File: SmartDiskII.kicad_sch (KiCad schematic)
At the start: 42 parts, among them J1 Apple II Expansion Slot, J2 DRV, U1 74LS174, U10 27C256, U11 74LS245, U12 74LS323, U13 74LS00, U14 74LS174, U2 NE556, U3 74LS05, U4 74LS132, U5 74LS259/9334, U6 74LS20, U7 74LS21, U8 2758/16/32 P6, U9 74LS30

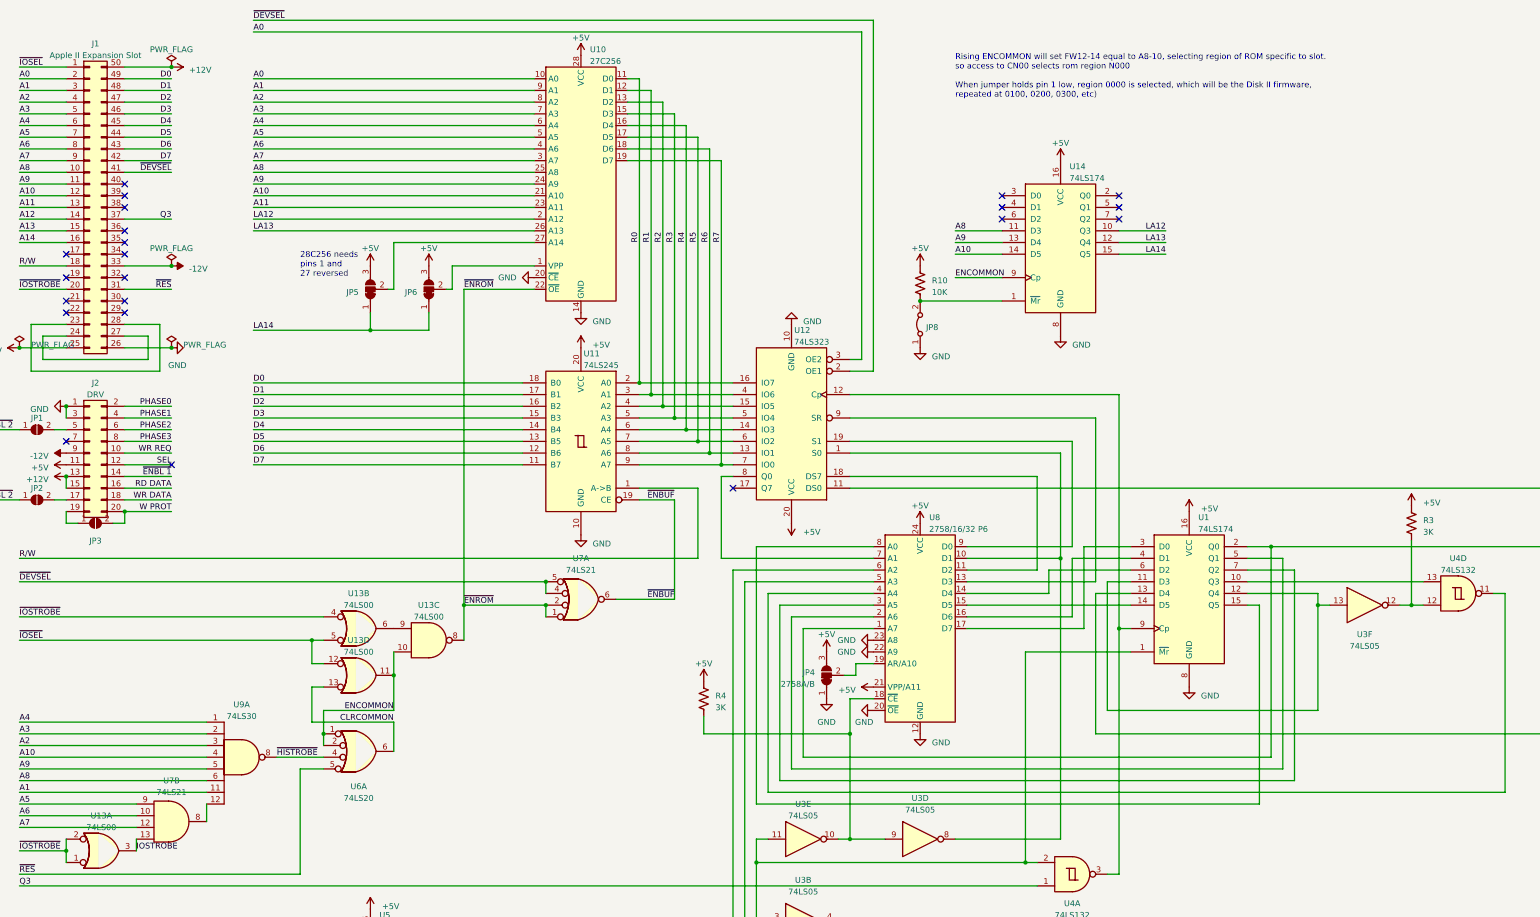
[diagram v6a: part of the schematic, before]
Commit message: fix jumper, tweaks
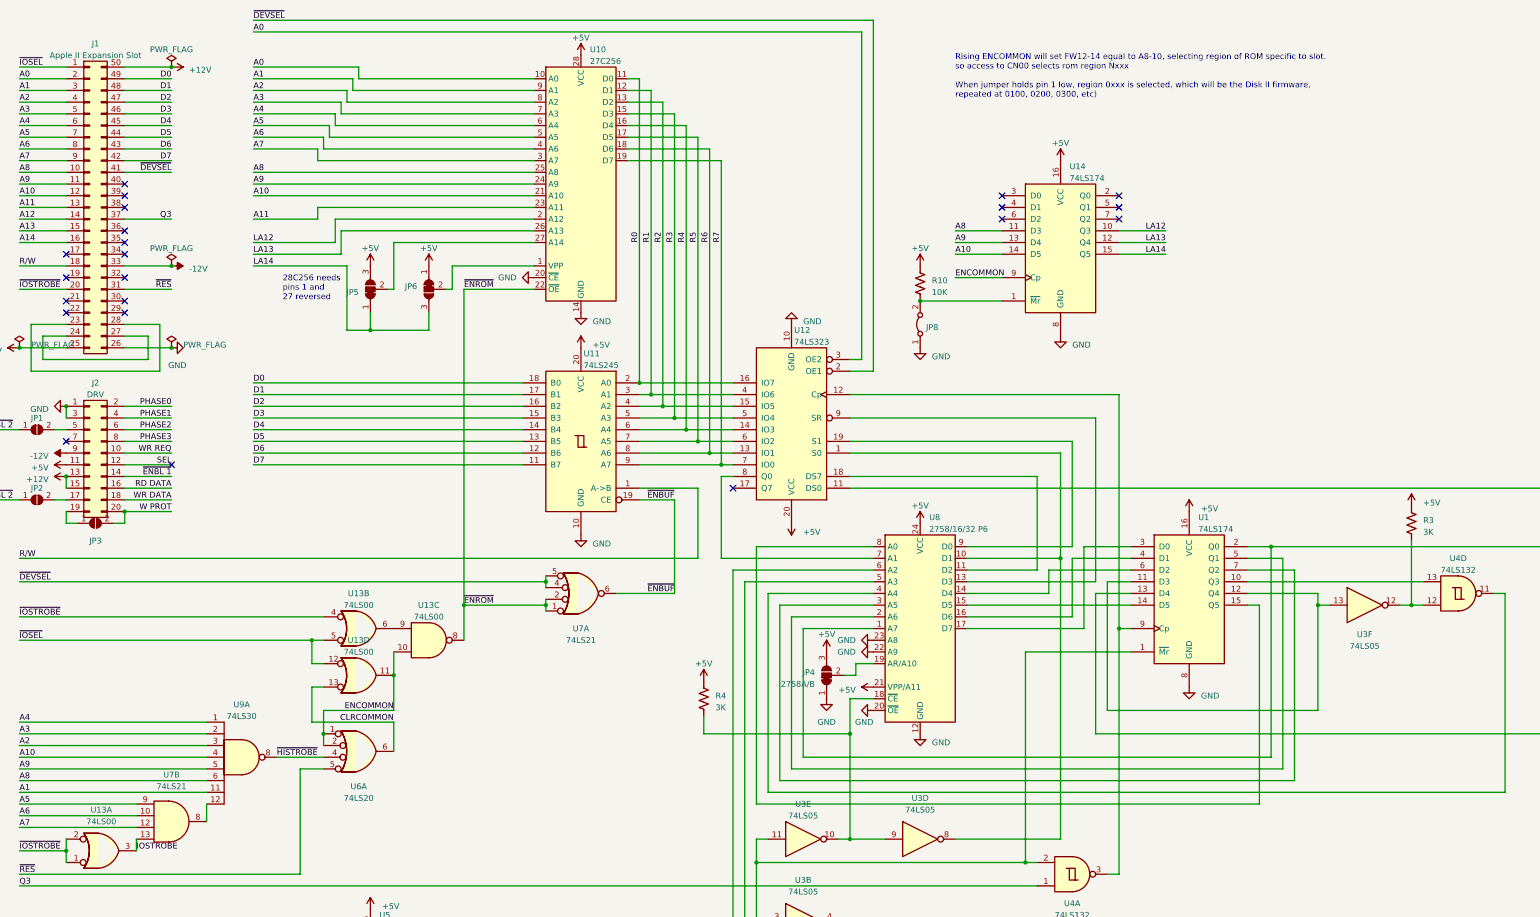
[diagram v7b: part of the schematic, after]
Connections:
- net +5V: now also JP6.1 (A); no longer JP6.3 (B)
- net LA14: now also JP6.3 (B); no longer JP6.1 (A)
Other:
- note added: "Rising ENCOMMON will set FW12-14 equal to A8-10, selecting region of ROM specific to slot. so access to CN00 selects rom region Nxxx When jumper holds pin 1 low, region 0xxx is selected, which will be the Disk II firmware, repeated at 0100, 0200, 0300, etc)"
- note removed: "Rising ENCOMMON will set FW12-14 equal to A8-10, selecting region of ROM specific to slot. so access to CN00 selects rom region N000 When jumper holds pin 1 low, region 0000 is selected, which will be the Disk II firmware, repeated at 0100, 0200, 0300, etc)"
- moved on the sheet: U7A

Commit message: Working circuit for multi-rom
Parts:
- added JP10: ~, Jumper:SolderJumper-2_P1.3mm_Open_RoundedPad1.0x1.5mm, symbol Jumper:SolderJumper_2_Open
- added JP7, JP9: ~, Jumper:SolderJumper-2_P1.3mm_Bridged_RoundedPad1.0x1.5mm, symbol Jumper:SolderJumper_2_Bridged
- JP8: value ~ -> DiskII Mode; symbol Jumper:Jumper_2_Bridged -> Jumper:Jumper_2_Open
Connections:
- net +5V: now also JP10.2 (B)
- net GND: now also JP7.1 (A), JP9.1 (A)
- net SEL: now also JP10.1 (A)
- net at J2.5 (Pin_5), JP1.2 (B): now also JP7.2 (B)
- net at J2.7 (Pin_7): now also JP9.2 (B)
- net LA12: no longer names the net of U10.2 (A12), U14.10 (Q3)
- net LA13: no longer names the net of U10.26 (A13), U14.12 (Q4)
- net LA14: no longer names the net of JP5.1 (A), JP6.3 (B), U14.15 (Q5)
- no-connect marks 27 -> 28
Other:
- note removed: "Rising ENCOMMON will set FW12-14 equal to A8-10, selecting region of ROM specific to slot. so access to CN00 selects rom region Nxxx When jumper holds pin 1 low, region 0xxx is selected, which will be the Disk II firmware, repeated at 0100, 0200, 0300, etc)"
- moved on the sheet: J1, J2, JP1, JP2, JP3, JP5, JP6, JP8, R10, U10, U11, U12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
